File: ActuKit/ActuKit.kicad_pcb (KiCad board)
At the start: 2 copper layers, 32 x 19 mm, 8 parts, among them J1 Conn_01x04_Pin, J2 Conn_01x04_Pin, Q1 2SC1815, U1 LD14-002, U2 BD6211

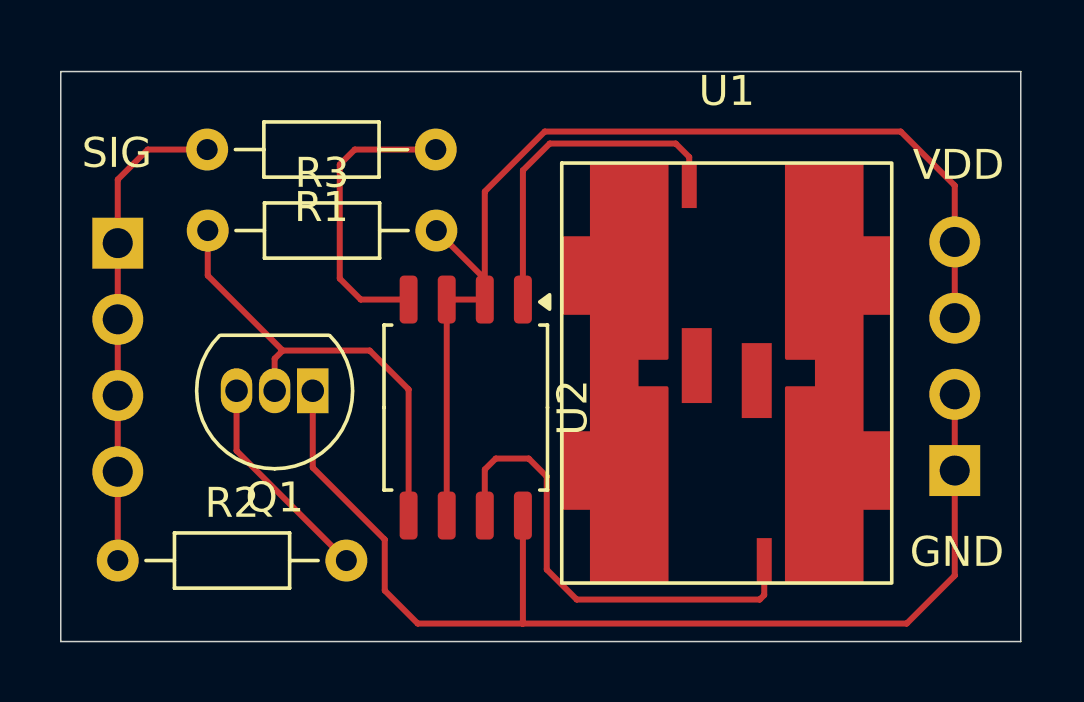
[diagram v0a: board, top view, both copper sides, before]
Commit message: [ActuKit] ミルピンのガイド用シルクの追加
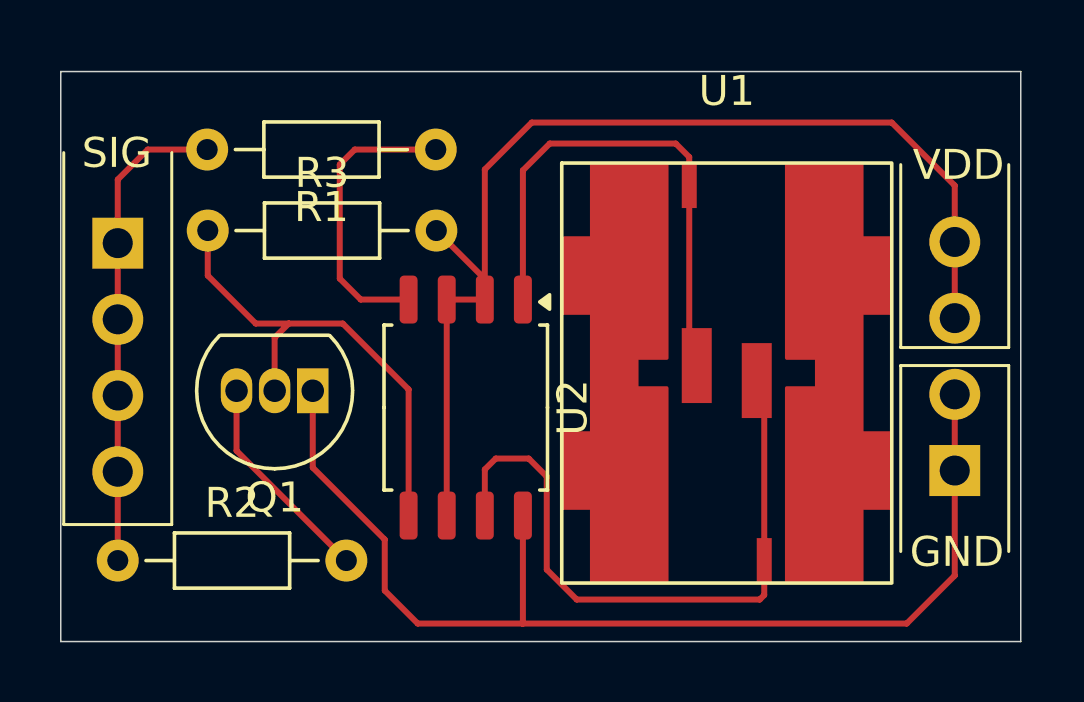
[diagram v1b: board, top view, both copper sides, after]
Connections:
- U1 pad 1: unconnected-(U1-INOUT1-Pad1) -> Net-(U1-INOUT1)
- U1 pad 2: unconnected-(U1-INOUT2-Pad2) -> Net-(U1-INOUT2)
- U1 pad 3: Net-(U1-INOUT3) -> Net-(U1-INOUT1)
- U1 pad 4: Net-(U1-INOUT4) -> Net-(U1-INOUT2)
- U2 pad 1: Net-(U1-INOUT3) -> Net-(U1-INOUT1)
- U2 pad 7: Net-(U1-INOUT4) -> Net-(U1-INOUT2)
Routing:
- net Net-(U1-INOUT2): track 0.00 -> 22.1 mm
- net Net-(U1-INOUT1): track 0.00 -> 17.5 mm
- net Net-(U1-INOUT4): track 16.0 -> 0.00 mm
- net Net-(U1-INOUT3): track 11.4 -> 0.00 mm
- net Net-(Q1-C): track 15.4 -> 16.4 mm
- net VDD: track 36.7 -> 37.4 mm
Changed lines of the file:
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@@
 			(layerselection 0x00010fc_ffffffff)
 			(plot_on_all_layers_selection 0x0000000_00000000)
-			(disableapertmacros no)
+			(disableapertmacros yes)
 			(usegerberextensions no)
 			(usegerberattributes yes)
@@
 	(net 5 "Net-(Q1-C)")
 	(net 6 "Net-(U2-FIN)")
-	(net 7 "Net-(U1-INOUT3)")
-	(net 8 "unconnected-(U1-INOUT2-Pad2)")
-	(net 9 "unconnected-(U1-INOUT1-Pad1)")
-	(net 10 "Net-(U1-INOUT4)")
+	(net 7 "Net-(U1-INOUT1)")
+	(net 8 "Net-(U1-INOUT2)")
 	(footprint "Package_SO:SOP-8_5.28x5.23mm_P1.27mm"
 		(layer "F.Cu")
@@
 			(layers "F.Cu" "F.Paste" "F.Mask")
 			(roundrect_rratio 0.25)
-			(net 7 "Net-(U1-INOUT3)")
+			(net 7 "Net-(U1-INOUT1)")
 			(pinfunction "OUT1")
 			(pintype "output")
@@
 			(layers "F.Cu" "F.Paste" "F.Mask")
 			(roundrect_rratio 0.25)
-			(net 10 "Net-(U1-INOUT4)")
+			(net 8 "Net-(U1-INOUT2)")
 			(pinfunction "OUT2")
 			(pintype "output")
@@
 			(size 1 2.5)
 			(layers "F.Cu" "F.Paste" "F.Mask")
-			(net 9 "unconnected-(U1-INOUT1-Pad1)")
+			(net 7 "Net-(U1-INOUT1)")
 			(pinfunction "INOUT1")
-			(pintype "bidirectional+no_connect")
+			(pintype "bidirectional")
 			(thermal_bridge_angle 45)
 		)
@@
 			(size 1 2.5)
 			(layers "F.Cu" "F.Paste" "F.Mask")
-			(net 8 "unconnected-(U1-INOUT2-Pad2)")
+			(net 8 "Net-(U1-INOUT2)")
 			(pinfunction "INOUT2")
-			(pintype "bidirectional+no_connect")
+			(pintype "bidirectional")
 			(thermal_bridge_angle 45)
 		)
@@
 			(size 0.5 1.5)
 			(layers "F.Cu" "F.Paste" "F.Mask")
-			(net 7 "Net-(U1-INOUT3)")
+			(net 7 "Net-(U1-INOUT1)")
 			(pinfunction "INOUT3")
 			(pintype "bidirectional")
@@
 			(size 0.5 1.5)
 			(layers "F.Cu" "F.Paste" "F.Mask")
-			(net 10 "Net-(U1-INOUT4)")
+			(net 8 "Net-(U1-INOUT2)")
 			(pinfunction "INOUT4")
 			(pintype "bidirectional")
@@
 		(tags "Resistor Axial_DIN0204 series Axial Horizontal pin pitch 7.62mm 0.167W length 3.6mm diameter 1.6mm")
 		(property "Reference" "R1"
-			(at 3.81 -1.92 360)
+			(at 3.81 -1.92 0)
 			(layer "F.SilkS")
 			(effects
@@
 		)
 		(property "Value" "20k"
-			(at 3.81 1.92 360)
+			(at 3.81 1.92 0)
 			(layer "F.Fab")
 			(effects
@@
 		)
 		(fp_text user "${REFERENCE}"
-			(at 3.81 0 360)
+			(at 3.81 0 0)
 			(layer "F.Fab")
 			(effects
@@
 		(tags "to-92 sc-43 sc-43a sot54 PA33 transistor")
 		(property "Reference" "Q1"
-			(at 1.27 -3.56 360)
+			(at 1.27 -3.56 0)
 			(layer "F.SilkS")
 			(effects
@@
 		)
 		(property "Value" "2SC1815"
-			(at 1.27 2.79 360)
+			(at 1.27 2.79 0)
 			(layer "F.Fab")
 			(effects
@@
 		)
 		(fp_text user "${REFERENCE}"
-			(at 1.27 0 360)
+			(at 1.27 0 0)
 			(layer "F.Fab")
 			(effects
@@
 		(tags "Resistor Axial_DIN0204 series Axial Horizontal pin pitch 7.62mm 0.167W length 3.6mm diameter 1.6mm")
 		(property "Reference" "R3"
-			(at 3.81 -1.92 360)
+			(at 3.81 -1.92 0)
 			(layer "F.SilkS")
 			(effects
@@
 		)
 		(property "Value" "20k"
-			(at 3.81 1.92 360)
+			(at 3.81 1.92 0)
 			(layer "F.Fab")
 			(effects
@@
 		)
 		(fp_text user "${REFERENCE}"
-			(at 3.81 0 360)
+			(at 3.81 0 0)
 			(layer "F.Fab")
 			(effects
@@
 	)
 	(gr_line
+		(start 157.3 109.2)
+		(end 160.9 109.2)
+		(stroke
+			(width 0.1)
+			(type default)
+		)
+		(layer "F.SilkS")
+	)
+	(gr_line
+		(start 160.9 108.6)
+		(end 160.9 102.5)
+		(stroke
+			(width 0.1)
+			(type default)
+		)
+		(layer "F.SilkS")
+	)
+	(gr_line
+		(start 160.9 109.2)
+		(end 160.9 115.4)
+		(stroke
+			(width 0.1)
+			(type default)
+		)
+		(layer "F.SilkS")
+	)
+	(gr_line
+		(start 129.4 102.1)
+		(end 129.4 114.5)
+		(stroke
+			(width 0.1)
+			(type default)
+		)
+		(layer "F.SilkS")
+	)
+	(gr_line
+		(start 157.3 102.5)
+		(end 157.3 108.6)
+		(stroke
+			(width 0.1)
+			(type default)
+		)
+		(layer "F.SilkS")
+	)
+	(gr_line
+		(start 133 114.5)
+		(end 133 102.1)
+		(stroke
+			(width 0.1)
+			(type default)
+		)
+		(layer "F.SilkS")
+	)
+	(gr_line
+		(start 157.3 115.4)
+		(end 157.3 109.2)
+		(stroke
+			(width 0.1)
+			(type default)
+		)
+		(layer "F.SilkS")
+	)
+	(gr_line
+		(start 129.4 114.5)
+		(end 133 114.5)
+		(stroke
+			(width 0.1)
+			(type default)
+		)
+		(layer "F.SilkS")
+	)
+	(gr_line
+		(start 157.3 108.6)
+		(end 160.9 108.6)
+		(stroke
+			(width 0.1)
+			(type default)
+		)
+		(layer "F.SilkS")
+	)
+	(gr_line
 		(start 161.3 99.4)
 		(end 161.3 118.4)
@@
 	)
 	(segment
-		(start 157.3 101.4)
-		(end 145.434314 101.4)
+		(start 157 101.1)
+		(end 145 101.1)
+		(width 0.2)
+		(layer "F.Cu")
+		(net 3)
+	)
+	(segment
+		(start 143.435 102.665)
+		(end 143.435 107)
+		(width 0.2)
+		(layer "F.Cu")
+		(net 3)
+	)
+	(segment
+		(start 159.1 103.2)
+		(end 157 101.1)
 		(width 0.2)
 		(layer "F.Cu")
@@
 	)
 	(segment
-		(start 145.434314 101.4)
-		(end 143.435 103.399314)
+		(start 145 101.1)
+		(end 143.435 102.665)
 		(width 0.2)
 		(layer "F.Cu")
@@
 	)
 	(segment
-		(start 143.435 103.399314)
-		(end 143.435 107)
+		(start 159.1 105.08)
+		(end 159.1 103.2)
 		(width 0.2)
 		(layer "F.Cu")
@@
 	)
 	(segment
-		(start 159.1 103.2)
-		(end 157.3 101.4)
-		(width 0.2)
-		(layer "F.Cu")
-		(net 3)
-	)
-	(segment
 		(start 141.82 104.7)
 		(end 143.435 106.315)
@@
 	)
 	(segment
-		(start 159.1 105.08)
-		(end 159.1 103.2)
-		(width 0.2)
-		(layer "F.Cu")
-		(net 3)
-	)
-	(segment
 		(start 138.82 115.7)
 		(end 135.16 112.04)
@@
 	)
 	(segment
-		(start 139.6 108.7)
+		(start 135.8 107.8)
+		(end 136.9 107.8)
+		(width 0.2)
+		(layer "F.Cu")
+		(net 5)
+	)
+	(segment
+		(start 138.7 107.8)
+		(end 136.9 107.8)
+		(width 0.2)
+		(layer "F.Cu")
+		(net 5)
+	)
+	(segment
+		(start 140.895 114.2)
 		(end 140.895 109.995)
 		(width 0.2)
@@
 	)
 	(segment
-		(start 140.895 109.995)
-		(end 140.895 114.2)
+		(start 136.9 107.8)
+		(end 136.43 108.27)
 		(width 0.2)
 		(layer "F.Cu")
@@
 	)
 	(segment
-		(start 136.43 108.97)
-		(end 136.7 108.7)
-		(width 0.2)
-		(layer "F.Cu")
-		(net 5)
-	)
-	(segment
-		(start 136.43 110.04)
-		(end 136.43 108.97)
-		(width 0.2)
-		(layer "F.Cu")
-		(net 5)
-	)
-	(segment
-		(start 136.7 108.7)
-		(end 139.6 108.7)
+		(start 134.2 106.2)
+		(end 135.8 107.8)
 		(width 0.2)
 		(layer "F.Cu")
@@
 	)
 	(segment
-		(start 134.2 106.2)
-		(end 136.7 108.7)
+		(start 136.43 108.27)
+		(end 136.43 110.04)
+		(width 0.2)
+		(layer "F.Cu")
+		(net 5)
+	)
+	(segment
+		(start 140.895 109.995)
+		(end 138.7 107.8)
 		(width 0.2)
 		(layer "F.Cu")
@@
 	(segment
 		(start 150.25 103.2)
+		(end 150.25 108.95)
+		(width 0.2)
+		(layer "F.Cu")
+		(net 7)
+	)
+	(segment
+		(start 150.25 108.95)
+		(end 150.5 109.2)
+		(width 0.2)
+		(layer "F.Cu")
+		(net 7)
+	)
+	(segment
+		(start 150.25 103.2)
 		(end 150.25 102.25)
 		(width 0.2)
@@
 		(width 0.2)
 		(layer "F.Cu")
-		(net 10)
+		(net 8)
 	)
 	(segment
@@
 		(width 0.2)
 		(layer "F.Cu")
-		(net 10)
+		(net 8)
 	)
 	(segment
@@
 		(width 0.2)
 		(layer "F.Cu")
-		(net 10)
+		(net 8)
+	)
+	(segment
+		(start 152.75 109.95)
+		(end 152.5 109.7)
+		(width 0.2)
+		(layer "F.Cu")
+		(net 8)
 	)
 	(segment
@@
 		(width 0.2)
 		(layer "F.Cu")
-		(net 10)
+		(net 8)
 	)
 	(segment
@@
 		(width 0.2)
 		(layer "F.Cu")
-		(net 10)
+		(net 8)
+	)
+	(segment
+		(start 152.75 115.7)
+		(end 152.75 109.95)
+		(width 0.2)
+		(layer "F.Cu")
+		(net 8)
 	)
 	(segment
@@
 		(width 0.2)
 		(layer "F.Cu")
-		(net 10)
+		(net 8)
 	)
 	(segment
@@
 		(width 0.2)
 		(layer "F.Cu")
-		(net 10)
+		(net 8)
 	)
 	(segment
@@
 		(width 0.2)
 		(layer "F.Cu")
-		(net 10)
+		(net 8)
 	)
 	(segment
@@
 		(width 0.2)
 		(layer "F.Cu")
-		(net 10)
+		(net 8)
 	)
 )

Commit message: [ActuKit] LD14-002のライブラリ更新に合わせた基板の変更
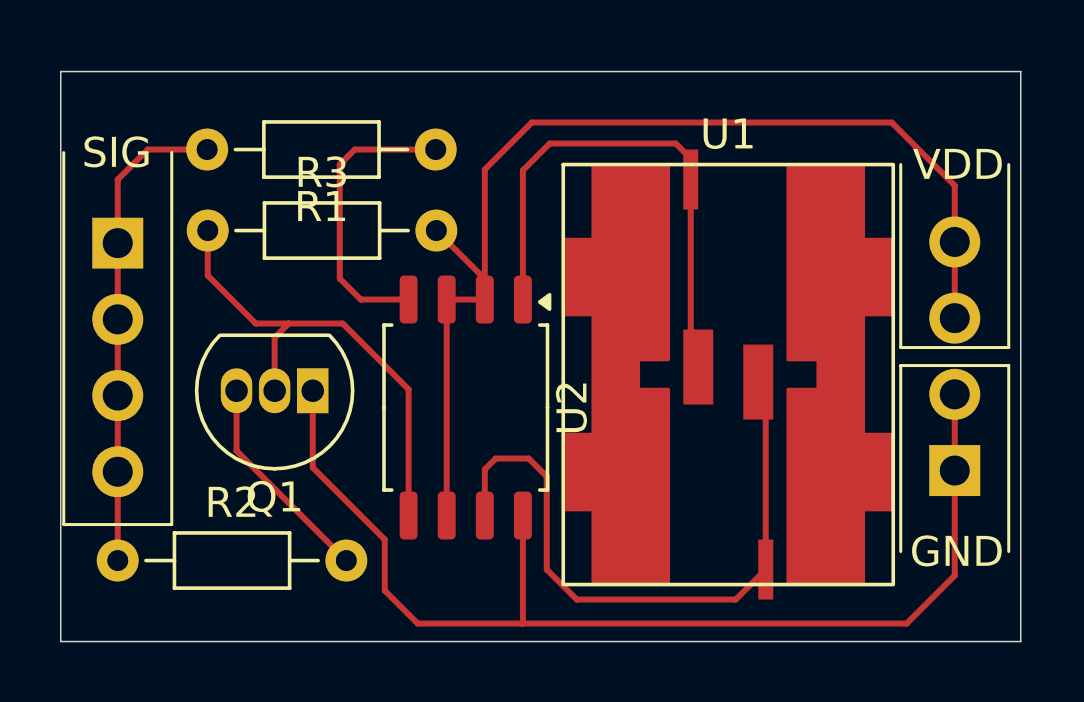
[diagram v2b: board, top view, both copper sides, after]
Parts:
- moved U1 0.07 mm to (151.6, 109.5)
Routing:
- net Net-(U1-INOUT1): track 17.5 -> 18.8 mm
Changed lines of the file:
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@@
-		)
-	)
-	(footprint "LT_Vibration_Actuator:LD14-002"
-		(layer "F.Cu")
-		(at 151.5 109.45)
-		(property "Reference" "U1"
-			(at 0 -9.4 0)
-			(unlocked yes)
-			(layer "F.SilkS")
-			(effects
-				(font
-					(size 1 1)
-					(thickness 0.15)
-				)
-			)
-		)
-		(property "Value" "LD14-002"
-			(at 0 -8 0)
-			(unlocked yes)
-			(layer "F.Fab")
-			(effects
-				(font
-					(size 1 1)
-					(thickness 0.15)
-				)
-			)
-		)
-		(property "Footprint" "LT_Vibration_Actuator:LD14-002"
-			(at 0 -17.7 0)
-			(unlocked yes)
-			(layer "F.Fab")
-			(hide yes)
-			(effects
-				(font
-					(size 1 1)
-					(thickness 0.15)
-				)
-			)
-		)
-		(property "Datasheet" "https://akizukidenshi.com/goodsaffix/LD14-002.png"
-			(at 0 -17.7 0)
-			(unlocked yes)
-			(layer "F.Fab")
-			(hide yes)
-			(effects
-				(font
-					(size 1 1)
-					(thickness 0.15)
-				)
-			)
-		)
-		(property "Description" ""
-			(at 0 -17.7 0)
-			(unlocked yes)
-			(layer "F.Fab")
-			(hide yes)
-			(effects
-				(font
-					(size 1 1)
-					(thickness 0.15)
-				)
-			)
-		)
-		(sheetname "ルート")
-		(sheetfile "ActuKit.kicad_sch")
-		(attr smd)
-		(fp_poly
-			(pts
-				(xy -4.5 6.95) (xy -2 6.95) (xy -2 0.5) (xy -3 0.5) (xy -3 -0.5) (xy -2 -0.5) (xy -2 -6.95) (xy -4.5 -6.95)
-				(xy -4.5 -4.5) (xy -5.45 -4.5) (xy -5.45 -2) (xy -4.5 -2) (xy -4.5 2) (xy -5.45 2) (xy -5.45 4.5)
-				(xy -4.5 4.5)
-			)
-			(stroke
-				(width 0.12)
-				(type solid)
-			)
-			(fill solid)
-			(layer "F.Cu")
-		)
-		(fp_poly
-			(pts
-				(xy 4.5 -6.95) (xy 2 -6.95) (xy 2 -0.5) (xy 3 -0.5) (xy 3 0.5) (xy 2 0.5) (xy 2 6.95) (xy 4.5 6.95)
-				(xy 4.5 4.5) (xy 5.45 4.5) (xy 5.45 2) (xy 4.5 2) (xy 4.5 -2) (xy 5.45 -2) (xy 5.45 -4.5) (xy 4.5 -4.5)
-			)
-			(stroke
-				(width 0.12)
-				(type solid)
-			)
-			(fill solid)
-			(layer "F.Cu")
-		)
-		(fp_rect
-			(start -5.5 -7)
-			(end 5.5 7)
-			(stroke
-				(width 0.12)
-				(type default)
-			)
-			(fill none)
-			(layer "F.SilkS")
-		)
-		(pad "1" smd rect
-			(at -1 -0.25)
-			(size 1 2.5)
-			(layers "F.Cu" "F.Paste" "F.Mask")
-			(net 7 "Net-(U1-INOUT1)")
-			(pinfunction "INOUT1")
-			(pintype "bidirectional")
-			(thermal_bridge_angle 45)
-		)
-		(pad "2" smd rect
-			(at 1 0.25)
-			(size 1 2.5)
-			(layers "F.Cu" "F.Paste" "F.Mask")
-			(net 8 "Net-(U1-INOUT2)")
-			(pinfunction "INOUT2")
-			(pintype "bidirectional")
-			(thermal_bridge_angle 45)
-		)
-		(pad "3" smd rect
-			(at -1.25 -6.25)
-			(size 0.5 1.5)
-			(layers "F.Cu" "F.Paste" "F.Mask")
-			(net 7 "Net-(U1-INOUT1)")
-			(pinfunction "INOUT3")
-			(pintype "bidirectional")
-			(thermal_bridge_angle 45)
-		)
-		(pad "4" smd rect
-			(at 1.25 6.25)
-			(size 0.5 1.5)
-			(layers "F.Cu" "F.Paste" "F.Mask")
-			(net 8 "Net-(U1-INOUT2)")
-			(pinfunction "INOUT4")
-			(pintype "bidirectional")
-			(thermal_bridge_angle 45)
-		)
-		(model "E:/Production/pcb-lab/liut-kicad-library/3dmodels/LD14-002.step"
-			(offset
-				(xyz 0 0 0)
-			)
-			(scale
-				(xyz 1 1 1)
-			)
-			(rotate
-				(xyz 0 0 0)
-			)
 		)
 	)
@@
 		)
 	)
+	(footprint "LT_Vibration_Actuator:LD14-002"
+		(layer "F.Cu")
+		(at 151.55 109.5)
+		(property "Reference" "U1"
+			(at 0 -8 0)
+			(unlocked yes)
+			(layer "F.SilkS")
+			(effects
+				(font
+					(size 1 1)
+					(thickness 0.15)
+				)
+			)
+		)
+		(property "Value" "LD14-002"
+			(at 0 7.9 0)
+			(unlocked yes)
+			(layer "F.Fab")
+			(effects
+				(font
+					(size 1 1)
+					(thickness 0.15)
+				)
+			)
+		)
+		(property "Footprint" "LT_Vibration_Actuator:LD14-002"
+			(at 0 -17.7 0)
+			(unlocked yes)
+			(layer "F.Fab")
+			(hide yes)
+			(effects
+				(font
+					(size 1 1)
+					(thickness 0.15)
+				)
+			)
+		)
+		(property "Datasheet" "https://akizukidenshi.com/goodsaffix/LD14-002.png"
+			(at 0 -17.7 0)
+			(unlocked yes)
+			(layer "F.Fab")
+			(hide yes)
+			(effects
+				(font
+					(size 1 1)
+					(thickness 0.15)
+				)
+			)
+		)
+		(property "Description" ""
+			(at 0 -17.7 0)
+			(unlocked yes)
+			(layer "F.Fab")
+			(hide yes)
+			(effects
+				(font
+					(size 1 1)
+					(thickness 0.15)
+				)
+			)
+		)
+		(sheetname "ルート")
+		(sheetfile "ActuKit.kicad_sch")
+		(attr smd)
+		(fp_poly
+			(pts
+				(xy -4.5 6.95) (xy -2 6.95) (xy -2 0.5) (xy -3 0.5) (xy -3 -0.5) (xy -2 -0.5) (xy -2 -6.95) (xy -4.5 -6.95)
+				(xy -4.5 -4.5) (xy -5.45 -4.5) (xy -5.45 -2) (xy -4.5 -2) (xy -4.5 2) (xy -5.45 2) (xy -5.45 4.5)
+				(xy -4.5 4.5)
+			)
+			(stroke
+				(width 0.12)
+				(type solid)
+			)
+			(fill solid)
+			(layer "F.Cu")
+		)
+		(fp_poly
+			(pts
+				(xy 4.5 -6.95) (xy 2 -6.95) (xy 2 -0.5) (xy 3 -0.5) (xy 3 0.5) (xy 2 0.5) (xy 2 6.95) (xy 4.5 6.95)
+				(xy 4.5 4.5) (xy 5.45 4.5) (xy 5.45 2) (xy 4.5 2) (xy 4.5 -2) (xy 5.45 -2) (xy 5.45 -4.5) (xy 4.5 -4.5)
+			)
+			(stroke
+				(width 0.12)
+				(type solid)
+			)
+			(fill solid)
+			(layer "F.Cu")
+		)
+		(fp_rect
+			(start -5.5 -7)
+			(end 5.5 7)
+			(stroke
+				(width 0.12)
+				(type default)
+			)
+			(fill none)
+			(layer "F.SilkS")
+		)
+		(pad "1" smd rect
+			(at -1 -0.25)
+			(size 1 2.5)
+			(layers "F.Cu" "F.Paste" "F.Mask")
+			(net 7 "Net-(U1-INOUT1)")
+			(pinfunction "INOUT1")
+			(pintype "bidirectional")
+			(thermal_bridge_angle 45)
+		)
+		(pad "2" smd rect
+			(at 1 0.25)
+			(size 1 2.5)
+			(layers "F.Cu" "F.Paste" "F.Mask")
+			(net 8 "Net-(U1-INOUT2)")
+			(pinfunction "INOUT2")
+			(pintype "bidirectional")
+			(thermal_bridge_angle 45)
+		)
+		(pad "3" smd rect
+			(at -1.25 -6.5)
+			(size 0.5 2)
+			(layers "F.Cu" "F.Paste" "F.Mask")
+			(net 7 "Net-(U1-INOUT1)")
+			(pinfunction "INOUT3")
+			(pintype "bidirectional")
+			(thermal_bridge_angle 45)
+		)
+		(pad "4" smd rect
+			(at 1.25 6.5)
+			(size 0.5 2)
+			(layers "F.Cu" "F.Paste" "F.Mask")
+			(net 8 "Net-(U1-INOUT2)")
+			(pinfunction "INOUT4")
+			(pintype "bidirectional")
+			(thermal_bridge_angle 45)
+		)
+		(model "E:/Production/pcb-lab/liut-kicad-library/3dmodels/LD14-002.step"
+			(offset
+				(xyz 0 0 0)
+			)
+			(scale
+				(xyz 1 1 1)
+			)
+			(rotate
+				(xyz 0 0 0)
+			)
+		)
+	)
 	(footprint "Connector_PinHeader_2.54mm:PinHeader_1x04_P2.54mm_Vertical"
 		(layer "B.Cu")
@@
 	)
 	(segment
-		(start 150.25 102.25)
-		(end 149.8 101.8)
+		(start 150.3 102.3)
+		(end 150.3 103)
 		(width 0.2)
 		(layer "F.Cu")
@@
 	)
 	(segment
-		(start 150.25 103.2)
-		(end 150.25 108.95)
+		(start 150.3 109)
+		(end 150.55 109.25)
+		(width 0.2)
+		(layer "F.Cu")
+		(net 7)
+	)
+	(segment
+		(start 150.3 103)
+		(end 150.3 109)
+		(width 0.2)
+		(layer "F.Cu")
+		(net 7)
+	)
+	(segment
+		(start 149.8 101.8)
+		(end 150.3 102.3)
 		(width 0.2)
 		(layer "F.Cu")
@@
 	)
 	(segment
+		(start 152.8 116)
+		(end 152.8 110)
+		(width 0.2)
+		(layer "F.Cu")
+		(net 8)
+	)
+	(segment
+		(start 152.8 110)
+		(end 152.55 109.75)
+		(width 0.2)
+		(layer "F.Cu")
+		(net 8)
+	)
+	(segment
 		(start 145.5 116)
 		(end 145.5 112.9)
@@
 	)
 	(segment
-		(start 152.75 109.95)
-		(end 152.5 109.7)
+		(start 146.5 117)
+		(end 151.8 117)
 		(width 0.2)
 		(layer "F.Cu")
@@
 	)
 	(segment
-		(start 152.75 115.7)
-		(end 152.75 109.95)
-		(width 0.2)
-		(layer "F.Cu")
-		(net 8)
-	)
-	(segment
-		(start 152.6 117)
-		(end 146.5 117)
-		(width 0.2)
-		(layer "F.Cu")
-		(net 8)
-	)
-	(segment
-		(start 152.75 116.85)
-		(end 152.6 117)
+		(start 151.8 117)
+		(end 152.8 116)
 		(width 0.2)
 		(layer "F.Cu")
@@
 		(width 0.2)
 		(layer "F.Cu")
-		(net 8)
-	)
-	(segment
-		(start 152.75 115.7)
-		(end 152.75 116.85)
-		(width 0.2)
-		(layer "F.Cu")
